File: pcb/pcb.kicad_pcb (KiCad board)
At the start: 2 copper layers, 284.6 x 110.1 mm, 175 parts, among them J1 USB_C_Receptacle_USB2.0, J2 USB_C_Receptacle_USB2.0, J4 USB_C_Receptacle_USB2.0, J5 USB_C_Receptacle_USB2.0, SW1 SW_Push, U1 SL2.1A, U2 NCP1117-3.3_SOT223, U3 W25Q128JVS, U4 RP2040, Y1 ABM8-272-T3

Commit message: Fixed Traces
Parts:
- removed REF**: Stabilizer_MX_6.25u, ScottoKeebs_Stabilizer:Stabilizer_MX_6.25u
- removed REF** (x3): Stabilizer_MX_2.00u, ScottoKeebs_Stabilizer:Stabilizer_MX_2.00u
- R6, R7, SW1, U4: moved to F.Cu
- U3: footprint Package_SO:SOIC-8_5.23x5.23mm_P1.27mm -> Package_SO:SOIC-8_5.3x5.3mm_P1.27mm
- moved U4 98.0 mm to (217.2, 110.0), turned to 90 degrees
- moved SW1 96.3 mm to (236.9, 110.5), turned to 0 degrees
- moved R7 90.3 mm to (210.6, 108.5), turned to 0 degrees
- moved R6 89.8 mm to (210.6, 109.7), turned to 0 degrees
- moved C16 37.6 mm to (187.0, 110.5), turned to 180 degrees
- moved C9 37.3 mm to (187.0, 107.0), turned to 180 degrees
- moved C14 37.0 mm to (187.0, 108.2), turned to 180 degrees
- moved C13 35.1 mm to (187.0, 116.5), turned to 180 degrees
- moved C15 31.9 mm to (187.0, 109.4), turned to 180 degrees
- moved C4 26.8 mm to (195.5, 107.0), turned to 180 degrees
- moved U2 22.9 mm to (192.9, 111.7)
- moved R5 21.3 mm to (224.9, 115.9)
- moved Y1 17.0 mm to (224.1, 113.0), turned to -90 degrees
- moved C1 16.1 mm to (224.5, 109.9)
- moved C8 16.0 mm to (208.2, 107.0)
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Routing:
- net col8: track 399.3 -> 94.0 mm, vias 5 -> 1
- net USBC_GND: track 598.8 -> 312.3 mm, vias 8 -> 2
- net col9: track 382.6 -> 116.3 mm, vias 5 -> 1
- net col10: track 366.3 -> 137.2 mm, vias 5 -> 1
- net row4: track 285.0 -> 509.1 mm
- net row3: track 282.8 -> 493.0 mm
- net row0: track 467.1 -> 269.7 mm
- net col11: track 352.1 -> 162.8 mm, vias 5 -> 1
- net col12: track 332.0 -> 150.5 mm, vias 4 -> 1
- net col7: track 393.0 -> 212.5 mm, vias 9 -> 1
- net +3V3: track 227.7 -> 73.2 mm, vias 5 -> 2
- net col13: track 306.2 -> 152.1 mm, vias 3 -> 1
- net /XIN: track 157.3 -> 5.96 mm, vias 5 -> 0
- net col6: track 356.1 -> 206.0 mm, vias 9 -> 1
- net +1V1: track 174.7 -> 32.3 mm, vias 7 -> 2
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
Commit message: Fixes
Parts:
- added REF**: Stabilizer_MX_6.25u, ScottoKeebs_Stabilizer:Stabilizer_MX_6.25u, F.Cu at (217.3, 200.8)
- added REF**: Stabilizer_MX_2.00u, ScottoKeebs_Stabilizer:Stabilizer_MX_2.00u, F.Cu at (341.1, 182.6)
- added REF**: Stabilizer_MX_2.00u, ScottoKeebs_Stabilizer:Stabilizer_MX_2.00u, F.Cu at (105.4, 181.7)
- added REF**: Stabilizer_MX_2.00u, ScottoKeebs_Stabilizer:Stabilizer_MX_2.00u, F.Cu at (345.9, 162.7)
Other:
- board text added: "Made By @CherryTree56567"
- board text removed: "Made By Ronit D'Silva @CherryTree56567"

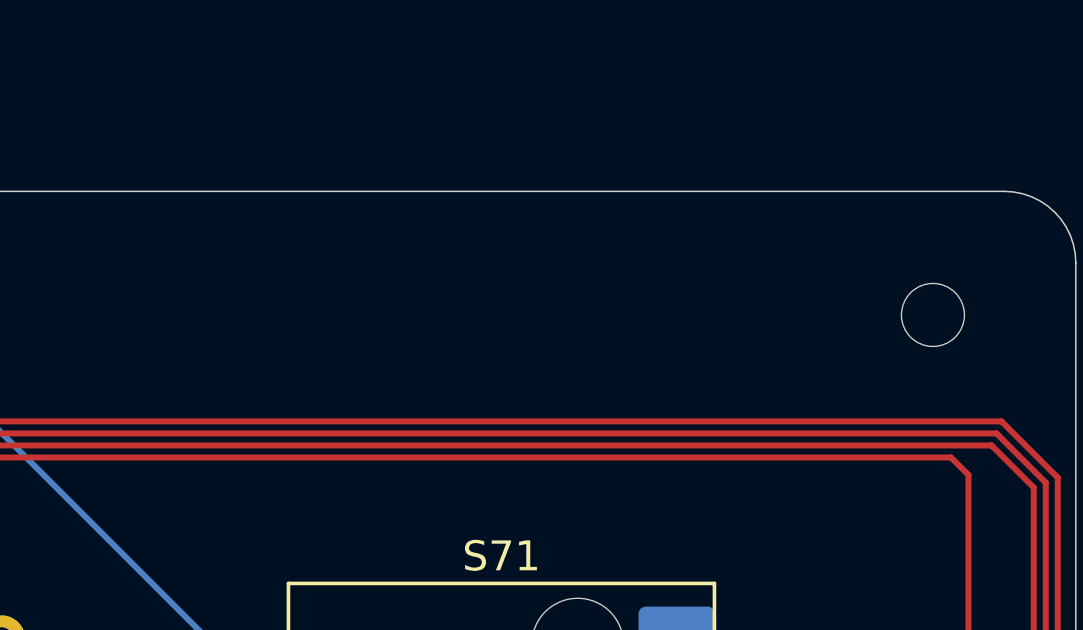
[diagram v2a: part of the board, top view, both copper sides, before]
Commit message: Added Silkscreen Username
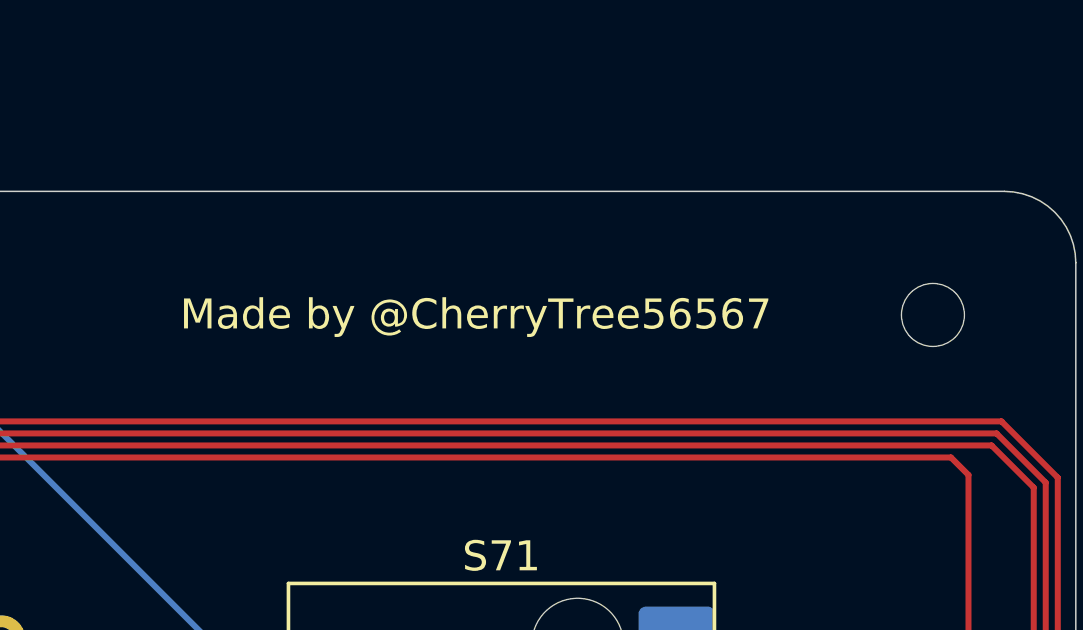
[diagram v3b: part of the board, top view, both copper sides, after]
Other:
- board text added: "Made by @CherryTree56567"
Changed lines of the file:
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@@
+		)
+	)
+	(gr_text "Made by @CherryTree56567"
+		(at 339.924088 109.94937 0)
+		(layer "F.SilkS")
+		(effects
+			(font
+				(size 1 1)
+				(thickness 0.1)
+			)
+			(justify left bottom)
 		)
 	)
